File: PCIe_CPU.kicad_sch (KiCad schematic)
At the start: 42 parts, among them J1 PCIe_x16_CPU, J6 Bus_M.2_Socket_M

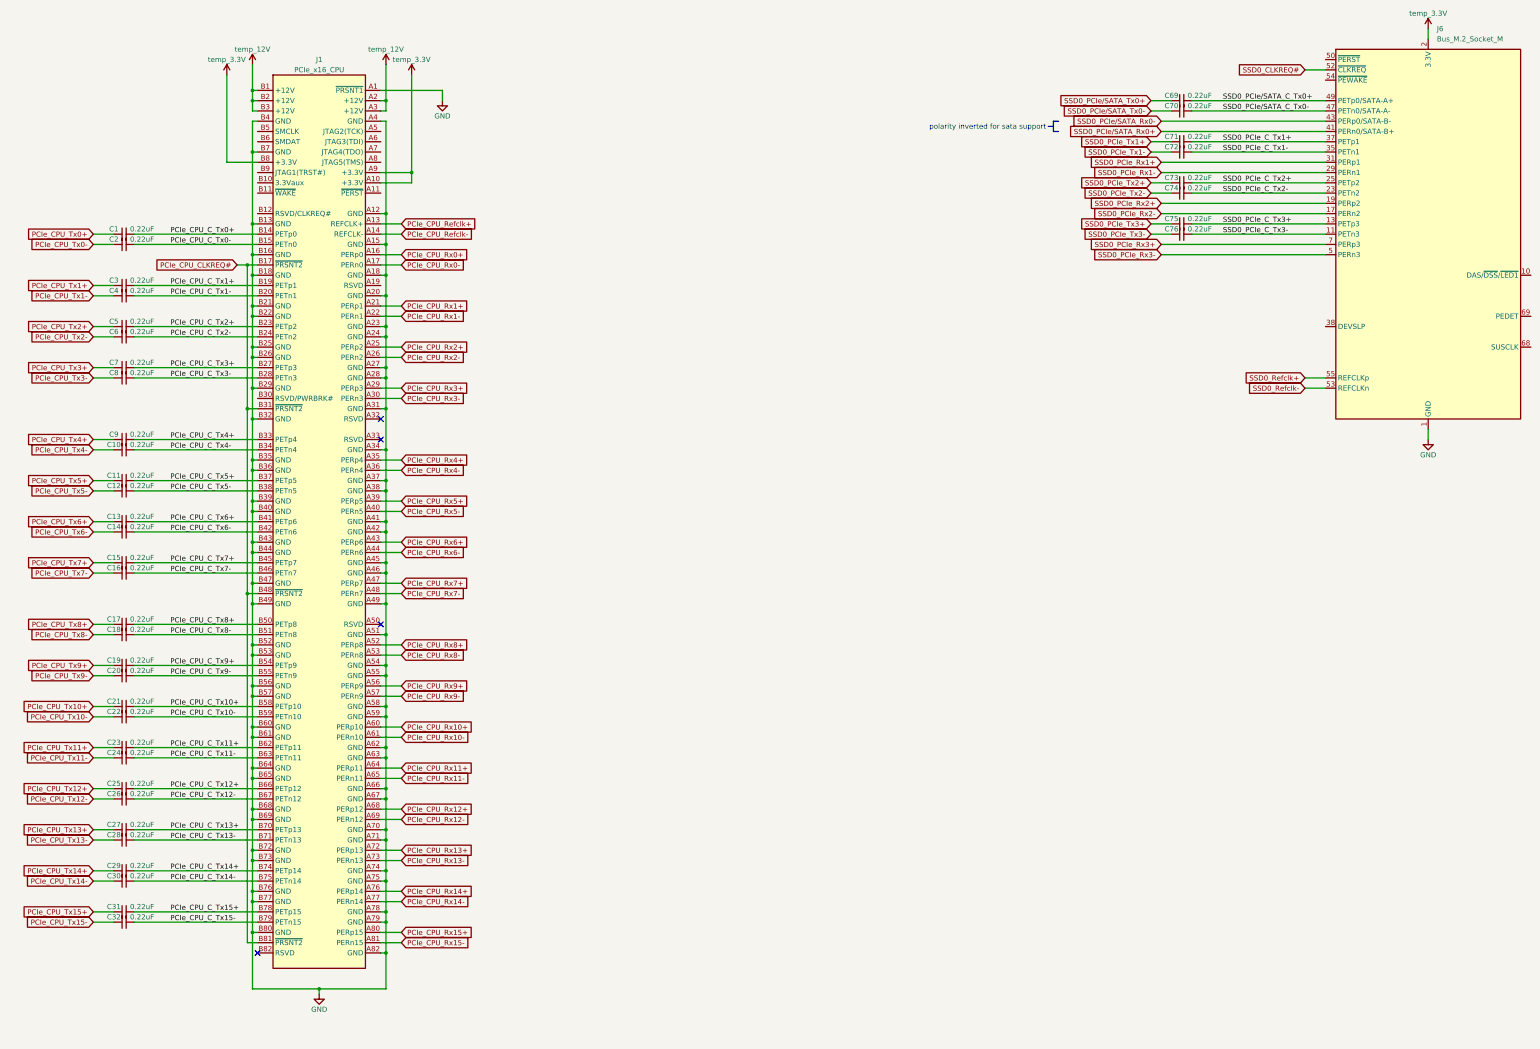
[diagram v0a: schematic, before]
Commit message: Restructured schematic
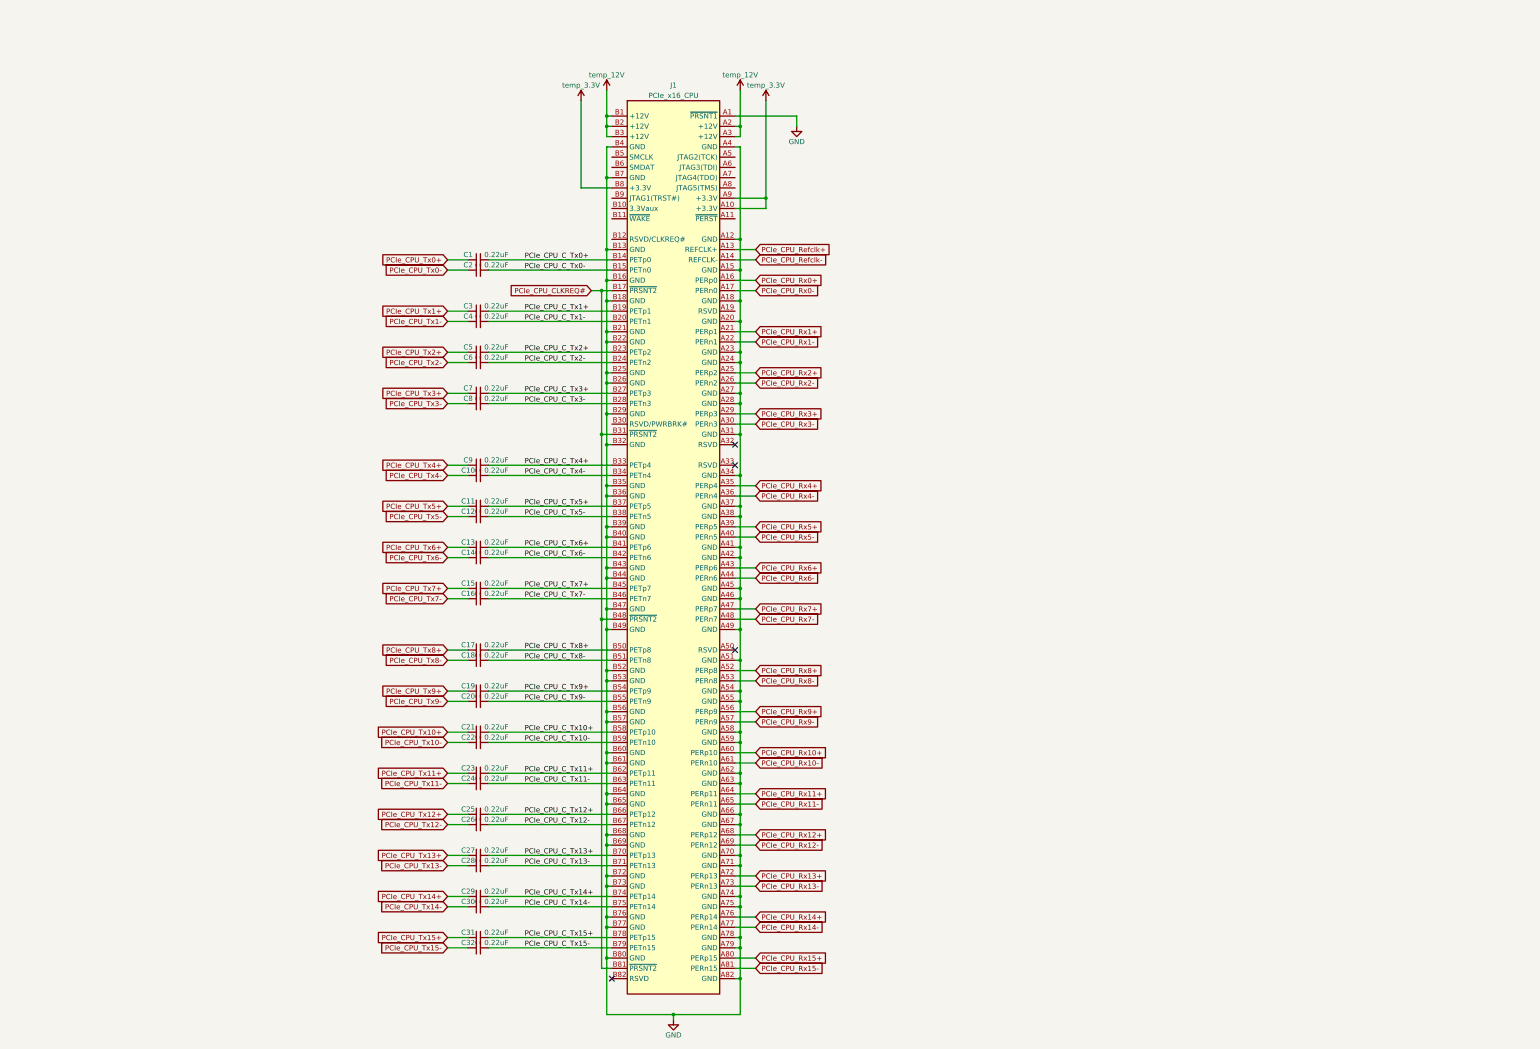
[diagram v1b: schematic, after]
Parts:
- removed C69, C70, C71, C72, C73, C74, C75, C76: 0.22uF, Capacitor_SMD:C_0402_1005Metric, symbol Device:C_Small
- removed J6: Bus_M.2_Socket_M, A-my-stuff:m-key, symbol Connector:Bus_M.2_Socket_M
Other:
- note removed: "polarity inverted for sata support"
- title: PCIe slots -> PCIe x16 slot from CPU
- moved on the sheet: C1, C10, C11, C12, C13, C14, C15, C16, C17, C18, C19, C2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
